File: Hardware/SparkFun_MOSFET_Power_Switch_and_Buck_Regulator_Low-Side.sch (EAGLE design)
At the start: 41 parts, among them J1 PTH, J3 5.5x2.1mm Barrel, J4 SMD, Q1 600mA/40V, Q2 100A/100V/6.8mΩ, U1 LMR14203

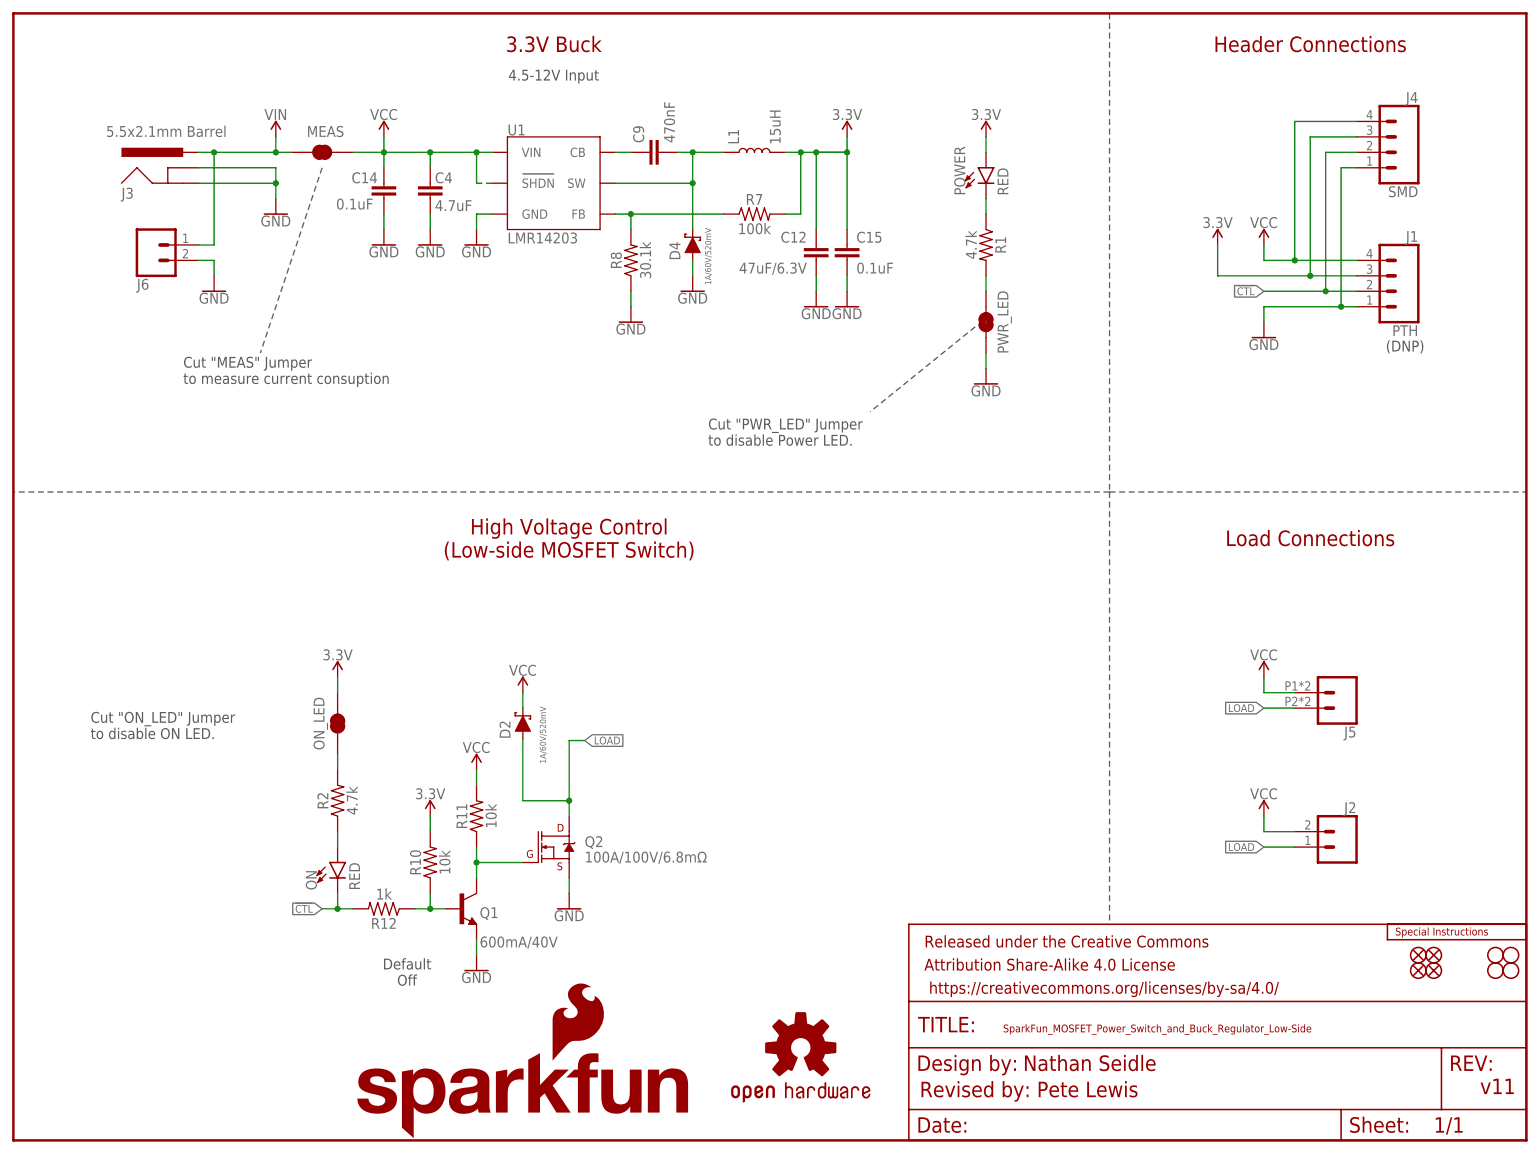
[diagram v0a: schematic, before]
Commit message: Added D1 Zener
-Added D1 to clamp spike on VCC and protect U1 and C4
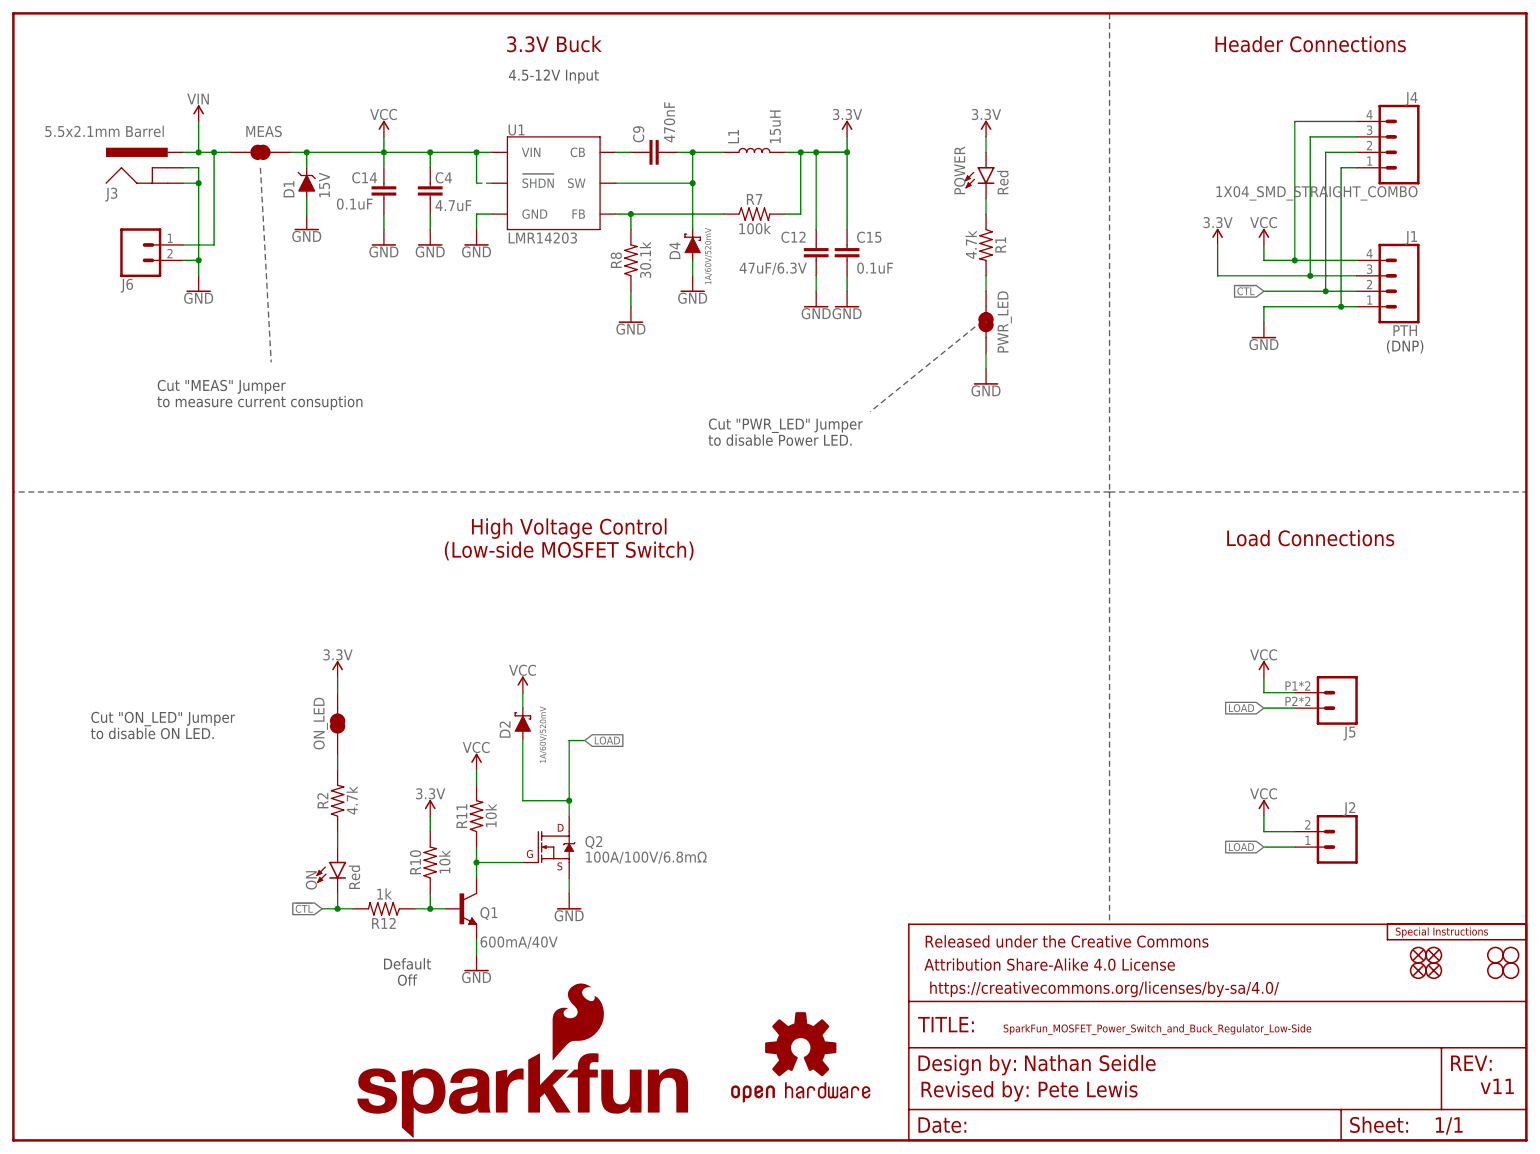
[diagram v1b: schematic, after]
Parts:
- added D1: 15V, SparkFun-DiscreteSemi:DIODE-ZENER-DZ2J150M0L
- J4: value SMD -> 1X04_SMD_STRAIGHT_COMBO
- ON, POWER: value RED -> Red
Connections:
- net GND: now also D1.A
- net VCC: now also D1.C
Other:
- moved on the sheet: J3, J6, MEAS
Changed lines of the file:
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@@
 <part name="H4" library="SparkFun-Hardware" deviceset="STAND-OFF" device=""/>
 <part name="H3" library="SparkFun-Hardware" deviceset="STAND-OFF" device=""/>
-<part name="ON" library="SparkFun-LED" deviceset="LED-RED" device="_0603-KB" value="RED"/>
+<part name="ON" library="SparkFun-LED" deviceset="LED-RED" device="_0603-KB" value="Red"/>
 <part name="R2" library="SparkFun-Resistors" deviceset="4.7KOHM" device="-0603-1/10W-1%" value="4.7k"/>
 <part name="R7" library="SparkFun-Resistors" deviceset="100KOHM" device="-0603-1/10W-1%" value="100k"/>
@@
 <part name="MEAS" library="SparkFun-Jumpers" deviceset="JUMPER-COMBO_2_NC_TRACE" device=""/>
 <part name="SUPPLY8" library="SparkFun-PowerSymbols" deviceset="3.3V" device=""/>
-<part name="POWER" library="SparkFun-LED" deviceset="LED-RED" device="_0603-KB" value="RED"/>
+<part name="POWER" library="SparkFun-LED" deviceset="LED-RED" device="_0603-KB" value="Red"/>
 <part name="R1" library="SparkFun-Resistors" deviceset="4.7KOHM" device="-0603-1/10W-1%" value="4.7k"/>
 <part name="GND2" library="SparkFun-PowerSymbols" deviceset="GND" device=""/>
-<part name="J4" library="SparkFun-Connectors" deviceset="CONN_04" device="SMD_STRAIGHT_COMBO" value="SMD"/>
+<part name="J4" library="SparkFun-Connectors" deviceset="CONN_04" device="SMD_STRAIGHT_COMBO" value="1X04_SMD_STRAIGHT_COMBO"/>
 <part name="LOGO2" library="SparkFun-Aesthetics" deviceset="SFE_LOGO_NAME_FLAME" device=".2_INCH" value="SFE_LOGO_NAME_FLAME.2_INCH"/>
 <part name="PWR_LED" library="SparkFun-Jumpers" deviceset="JUMPER-SMT_2_NC_TRACE" device="_SILK" package3d_urn="urn:adsk.eagle:package:39281/1" value=""/>
@@
 <part name="LOGO3" library="SparkFun-Aesthetics" deviceset="SPECIAL_INSTRUCTIONS" device="-ORDERING"/>
 <part name="SUPPLY1" library="SparkFun-PowerSymbols" deviceset="3.3V" device=""/>
+<part name="D1" library="SparkFun-DiscreteSemi" deviceset="DIODE-ZENER" device="-DZ2J150M0L" value="15V"/>
 </parts>
 <sheets>
@@
 <wire x1="158.242" y1="133.858" x2="140.97" y2="119.888" width="0.1524" layer="97" style="shortdash"/>
 <text x="232.156" y="131.572" size="1.778" layer="97" font="vector" rot="R180">(DNP)</text>
-<text x="27.94" y="124.46" size="1.778" layer="97" font="vector">Cut "MEAS" Jumper
+<text x="23.622" y="120.65" size="1.778" layer="97" font="vector">Cut "MEAS" Jumper
 to measure current consuption</text>
-<wire x1="50.8" y1="160.02" x2="40.64" y2="129.54" width="0.1524" layer="97" style="shortdash"/>
+<wire x1="40.64" y1="160.02" x2="42.418" y2="128.016" width="0.1524" layer="97" style="shortdash"/>
 </plain>
 <instances>
@@
 <attribute name="VALUE" x="86.614" y="61.976" size="1.016" layer="96" font="vector" rot="R90" align="top-left"/>
 </instance>
-<instance part="GND11" gate="1" x="43.18" y="152.4" smashed="yes">
-<attribute name="VALUE" x="43.18" y="152.146" size="1.778" layer="96" font="vector" align="top-center"/>
-</instance>
-<instance part="J3" gate="G$1" x="27.94" y="154.94" smashed="yes">
-<attribute name="VALUE" x="15.24" y="165.1" size="1.778" layer="96" font="vector"/>
-<attribute name="NAME" x="17.78" y="154.94" size="1.778" layer="95" font="vector"/>
+<instance part="GND11" gate="1" x="48.26" y="149.86" smashed="yes">
+<attribute name="VALUE" x="48.26" y="149.606" size="1.778" layer="96" font="vector" align="top-center"/>
+</instance>
+<instance part="J3" gate="G$1" x="25.4" y="154.94" smashed="yes">
+<attribute name="VALUE" x="5.08" y="165.1" size="1.778" layer="96" font="vector"/>
+<attribute name="NAME" x="15.24" y="154.94" size="1.778" layer="95" font="vector"/>
 </instance>
 <instance part="J5" gate="J1" x="218.44" y="73.66" smashed="yes" rot="R180">
@@
 <attribute name="NAME" x="220.98" y="68.072" size="1.778" layer="95" font="vector" rot="R180"/>
 </instance>
-<instance part="SUPPLY3" gate="G$1" x="43.18" y="165.1" smashed="yes">
-<attribute name="VALUE" x="43.18" y="167.894" size="1.778" layer="96" font="vector" align="bottom-center"/>
+<instance part="SUPPLY3" gate="G$1" x="30.48" y="167.64" smashed="yes">
+<attribute name="VALUE" x="30.48" y="170.434" size="1.778" layer="96" font="vector" align="bottom-center"/>
 </instance>
 <instance part="SUPPLY4" gate="G$1" x="60.96" y="165.1" smashed="yes">
@@
 <attribute name="VALUE" x="205.74" y="56.134" size="1.778" layer="96" font="vector" align="bottom-center"/>
 </instance>
-<instance part="MEAS" gate="JP1" x="50.8" y="162.56" smashed="yes">
-<attribute name="NAME" x="48.26" y="165.1" size="1.778" layer="95" font="vector"/>
+<instance part="MEAS" gate="JP1" x="40.64" y="162.56" smashed="yes">
+<attribute name="NAME" x="38.1" y="165.1" size="1.778" layer="95" font="vector"/>
 </instance>
 <instance part="SUPPLY8" gate="G$1" x="160.02" y="165.1" smashed="yes">
@@
 <instance part="FD3" gate="G$1" x="231.14" y="27.94" smashed="yes"/>
 <instance part="FD4" gate="G$1" x="233.68" y="27.94" smashed="yes"/>
-<instance part="J6" gate="J1" x="22.86" y="147.32" smashed="yes" rot="MR180">
-<attribute name="VALUE" x="20.32" y="152.146" size="1.778" layer="96" font="vector" rot="MR180"/>
-<attribute name="NAME" x="20.32" y="141.732" size="1.778" layer="95" font="vector" rot="MR180"/>
-</instance>
-<instance part="GND3" gate="1" x="33.02" y="139.7" smashed="yes">
-<attribute name="VALUE" x="33.02" y="139.446" size="1.778" layer="96" font="vector" align="top-center"/>
+<instance part="J6" gate="J1" x="20.32" y="147.32" smashed="yes" rot="MR180">
+<attribute name="VALUE" x="17.78" y="152.146" size="1.778" layer="96" font="vector" rot="MR180"/>
+<attribute name="NAME" x="17.78" y="141.732" size="1.778" layer="95" font="vector" rot="MR180"/>
+</instance>
+<instance part="GND3" gate="1" x="30.48" y="139.7" smashed="yes">
+<attribute name="VALUE" x="30.48" y="139.446" size="1.778" layer="96" font="vector" align="top-center"/>
 </instance>
 <instance part="LOGO3" gate="G$1" x="226.06" y="33.02" smashed="yes"/>
 <instance part="SUPPLY1" gate="G$1" x="53.34" y="76.2" smashed="yes">
 <attribute name="VALUE" x="53.34" y="78.994" size="1.778" layer="96" font="vector" align="bottom-center"/>
+</instance>
+<instance part="D1" gate="G$1" x="48.26" y="157.48" smashed="yes" rot="R90">
+<attribute name="NAME" x="46.228" y="154.94" size="1.778" layer="95" font="vector" rot="R90"/>
+<attribute name="VALUE" x="50.292" y="154.94" size="1.778" layer="96" font="vector" rot="R90" align="top-left"/>
 </instance>
 </instances>
@@
 </segment>
 <segment>
-<wire x1="30.48" y1="157.48" x2="43.18" y2="157.48" width="0.1524" layer="91"/>
-<wire x1="43.18" y1="157.48" x2="43.18" y2="154.94" width="0.1524" layer="91"/>
-<wire x1="30.48" y1="160.02" x2="43.18" y2="160.02" width="0.1524" layer="91"/>
-<wire x1="43.18" y1="160.02" x2="43.18" y2="157.48" width="0.1524" layer="91"/>
-<junction x="43.18" y="157.48"/>
-<pinref part="GND11" gate="1" pin="GND"/>
+<wire x1="27.94" y1="157.48" x2="30.48" y2="157.48" width="0.1524" layer="91"/>
+<wire x1="27.94" y1="160.02" x2="30.48" y2="160.02" width="0.1524" layer="91"/>
 <pinref part="J3" gate="G$1" pin="GNDBREAK"/>
 <pinref part="J3" gate="G$1" pin="GND"/>
+<wire x1="30.48" y1="157.48" x2="30.48" y2="144.78" width="0.1524" layer="91"/>
+<junction x="30.48" y="157.48"/>
+<pinref part="J6" gate="J1" pin="2"/>
+<wire x1="27.94" y1="144.78" x2="30.48" y2="144.78" width="0.1524" layer="91"/>
+<pinref part="GND3" gate="1" pin="GND"/>
+<wire x1="30.48" y1="144.78" x2="30.48" y2="142.24" width="0.1524" layer="91"/>
+<junction x="30.48" y="144.78"/>
+<wire x1="30.48" y1="160.02" x2="30.48" y2="157.48" width="0.1524" layer="91"/>
 </segment>
 <segment>
@@
 </segment>
 <segment>
-<pinref part="J6" gate="J1" pin="2"/>
-<wire x1="30.48" y1="144.78" x2="33.02" y2="144.78" width="0.1524" layer="91"/>
-<pinref part="GND3" gate="1" pin="GND"/>
-<wire x1="33.02" y1="144.78" x2="33.02" y2="142.24" width="0.1524" layer="91"/>
+<pinref part="D1" gate="G$1" pin="A"/>
+<pinref part="GND11" gate="1" pin="GND"/>
+<wire x1="48.26" y1="152.4" x2="48.26" y2="154.94" width="0.1524" layer="91"/>
 </segment>
 </net>
@@
 <net name="VIN" class="0">
 <segment>
-<wire x1="45.72" y1="162.56" x2="43.18" y2="162.56" width="0.1524" layer="91"/>
-<wire x1="43.18" y1="162.56" x2="43.18" y2="165.1" width="0.1524" layer="91"/>
-<wire x1="30.48" y1="162.56" x2="33.02" y2="162.56" width="0.1524" layer="91"/>
-<junction x="43.18" y="162.56"/>
+<wire x1="27.94" y1="162.56" x2="30.48" y2="162.56" width="0.1524" layer="91"/>
 <pinref part="J3" gate="G$1" pin="PWR"/>
 <pinref part="SUPPLY3" gate="G$1" pin="VIN"/>
 <pinref part="MEAS" gate="JP1" pin="1"/>
-<wire x1="33.02" y1="162.56" x2="43.18" y2="162.56" width="0.1524" layer="91"/>
+<wire x1="30.48" y1="162.56" x2="33.02" y2="162.56" width="0.1524" layer="91"/>
+<wire x1="33.02" y1="162.56" x2="35.56" y2="162.56" width="0.1524" layer="91"/>
 <wire x1="33.02" y1="162.56" x2="33.02" y2="147.32" width="0.1524" layer="91"/>
 <junction x="33.02" y="162.56"/>
 <pinref part="J6" gate="J1" pin="1"/>
-<wire x1="33.02" y1="147.32" x2="30.48" y2="147.32" width="0.1524" layer="91"/>
+<wire x1="33.02" y1="147.32" x2="27.94" y2="147.32" width="0.1524" layer="91"/>
+<wire x1="30.48" y1="162.56" x2="30.48" y2="167.64" width="0.1524" layer="91"/>
+<junction x="30.48" y="162.56"/>
 </segment>
 </net>
@@
 <pinref part="U1" gate="U1" pin="SHDN"/>
 <pinref part="U1" gate="U1" pin="VIN"/>
-<wire x1="55.88" y1="162.56" x2="60.96" y2="162.56" width="0.1524" layer="91"/>
+<wire x1="45.72" y1="162.56" x2="48.26" y2="162.56" width="0.1524" layer="91"/>
 <junction x="60.96" y="162.56"/>
+<wire x1="48.26" y1="162.56" x2="60.96" y2="162.56" width="0.1524" layer="91"/>
 <wire x1="60.96" y1="165.1" x2="60.96" y2="162.56" width="0.1524" layer="91"/>
 <pinref part="SUPPLY4" gate="G$1" pin="VCC"/>
 <pinref part="MEAS" gate="JP1" pin="2"/>
-</segment>
-<segment>
+<pinref part="D1" gate="G$1" pin="C"/>
+<wire x1="48.26" y1="160.02" x2="48.26" y2="162.56" width="0.1524" layer="91"/>
+<junction x="48.26" y="162.56"/>
+</segment>
+<segment>

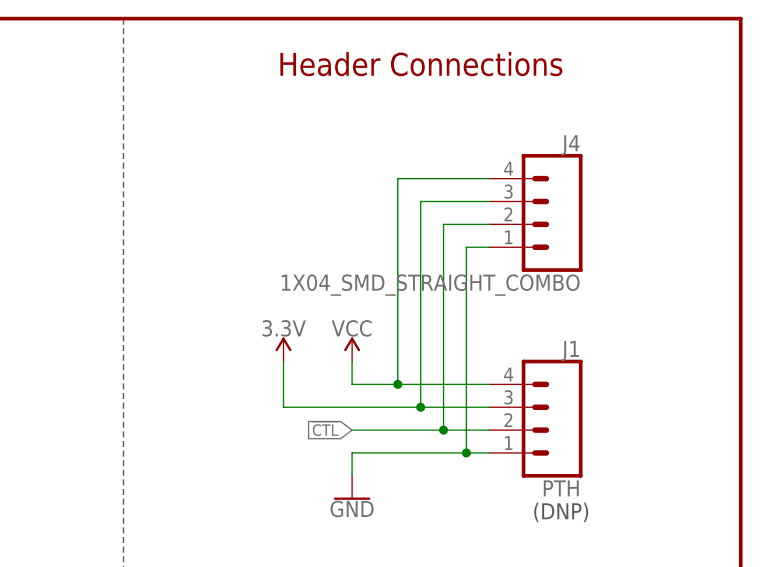
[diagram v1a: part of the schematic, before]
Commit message: text overlap in sch
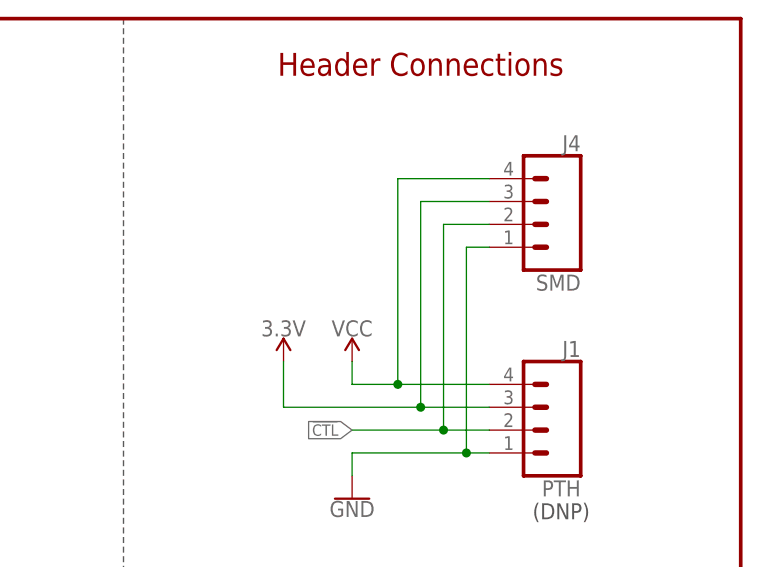
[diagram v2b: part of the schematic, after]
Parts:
- J4: value 1X04_SMD_STRAIGHT_COMBO -> SMD
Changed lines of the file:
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@@
 <part name="R1" library="SparkFun-Resistors" deviceset="4.7KOHM" device="-0603-1/10W-1%" value="4.7k"/>
 <part name="GND2" library="SparkFun-PowerSymbols" deviceset="GND" device=""/>
-<part name="J4" library="SparkFun-Connectors" deviceset="CONN_04" device="SMD_STRAIGHT_COMBO" value="1X04_SMD_STRAIGHT_COMBO"/>
+<part name="J4" library="SparkFun-Connectors" deviceset="CONN_04" device="SMD_STRAIGHT_COMBO" value="SMD"/>
 <part name="LOGO2" library="SparkFun-Aesthetics" deviceset="SFE_LOGO_NAME_FLAME" device=".2_INCH" value="SFE_LOGO_NAME_FLAME.2_INCH"/>
 <part name="PWR_LED" library="SparkFun-Jumpers" deviceset="JUMPER-SMT_2_NC_TRACE" device="_SILK" package3d_urn="urn:adsk.eagle:package:39281/1" value=""/>
